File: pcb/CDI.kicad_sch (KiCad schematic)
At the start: 27 parts, among them Q1 MMBT2222A, Q5 MMBT2222A, Q6 MMBT2222A

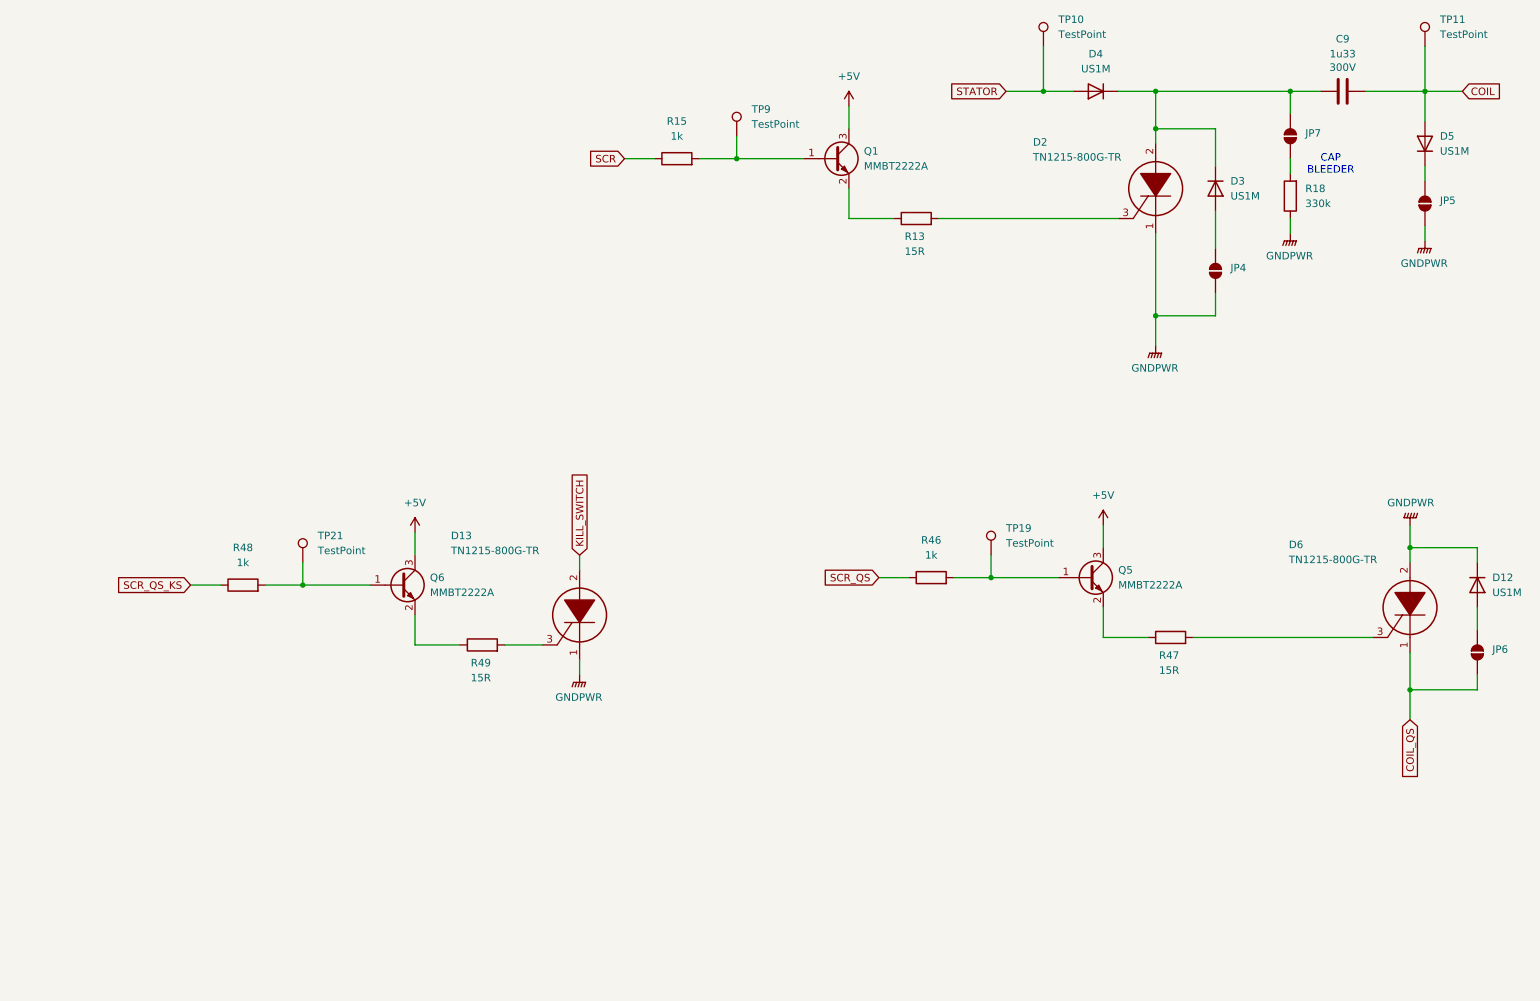
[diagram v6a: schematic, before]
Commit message: changed SCR drives to pnp drive and started schematic revision
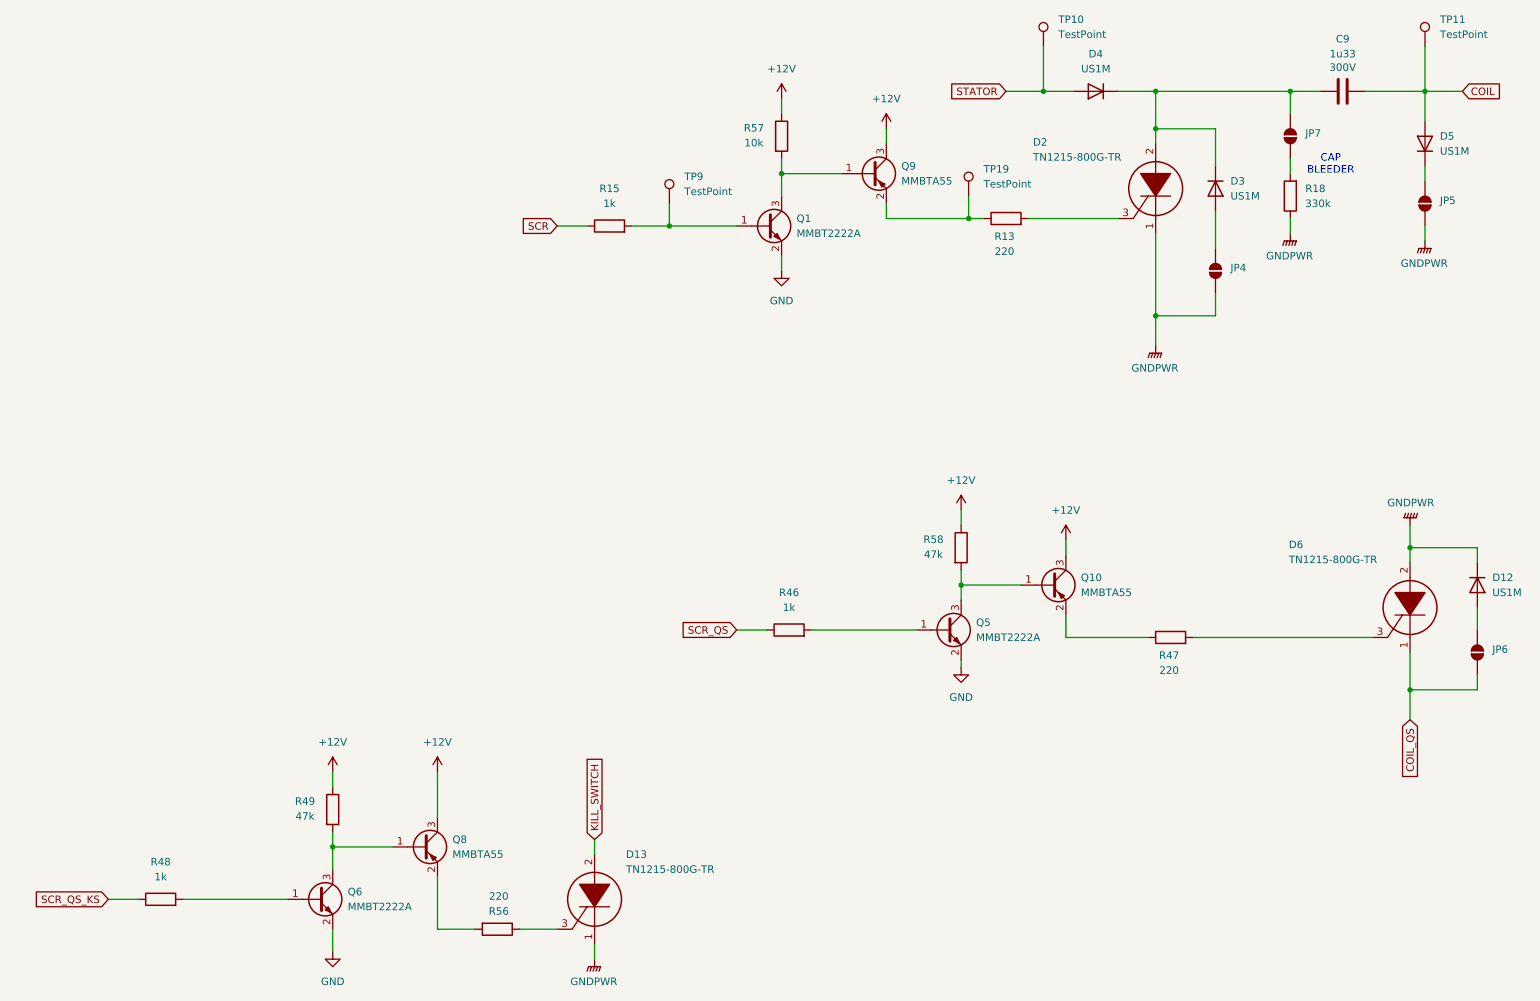
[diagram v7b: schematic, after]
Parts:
- removed TP21: TestPoint, Connector_PinHeader_1.00mm:PinHeader_1x01_P1.00mm_Vertical, symbol Connector:TestPoint
- added Q10, Q8, Q9: MMBTA55, Package_TO_SOT_SMD:SOT-23, symbol Transistor_BJT:MMBTA56
- added R56: 220, Resistor_THT:R_Axial_DIN0204_L3.6mm_D1.6mm_P1.90mm_Vertical, symbol Device:R
- added R57: 10k, Resistor_THT:R_Axial_DIN0204_L3.6mm_D1.6mm_P1.90mm_Vertical, symbol Device:R
- added R58: 47k, Resistor_THT:R_Axial_DIN0204_L3.6mm_D1.6mm_P1.90mm_Vertical, symbol Device:R
- R13, R47: value 15R -> 220
- R49: value 15R -> 47k
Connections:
- net at D13.3: now also R56.1; no longer R49.2
- net +12V: now reaches R49.1
- net +12V: now also Q10.3 (C), Q8.3 (C), Q9.3 (C), R57.1, R58.1; no longer Q6.2 (E)
- net at Q5.1 (B), R46.2: no longer TP19.1
- net at R47.1: now also Q10.2 (E); no longer Q5.2 (E)
- net at R13.1: now also TP19.1, Q9.2 (E); no longer Q1.2 (E)
- removed net +5V: Q1.3 (C), Q5.3 (C), Q6.3 (C)
- new net: Q1.3 (C), Q9.1 (B), R57.2
- new net: Q6.3 (C), Q8.1 (B), R49.2
- new net: Q8.2 (E), R56.2
- new net: Q10.1 (B), Q5.3 (C), R58.2
- new net GND: Q1.2 (E), Q5.2 (E), Q6.2 (E)
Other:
- moved on the sheet: D13, Q1, Q5, Q6, R13, R15, R46, R48, TP19, TP9

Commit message: completed photomos revision
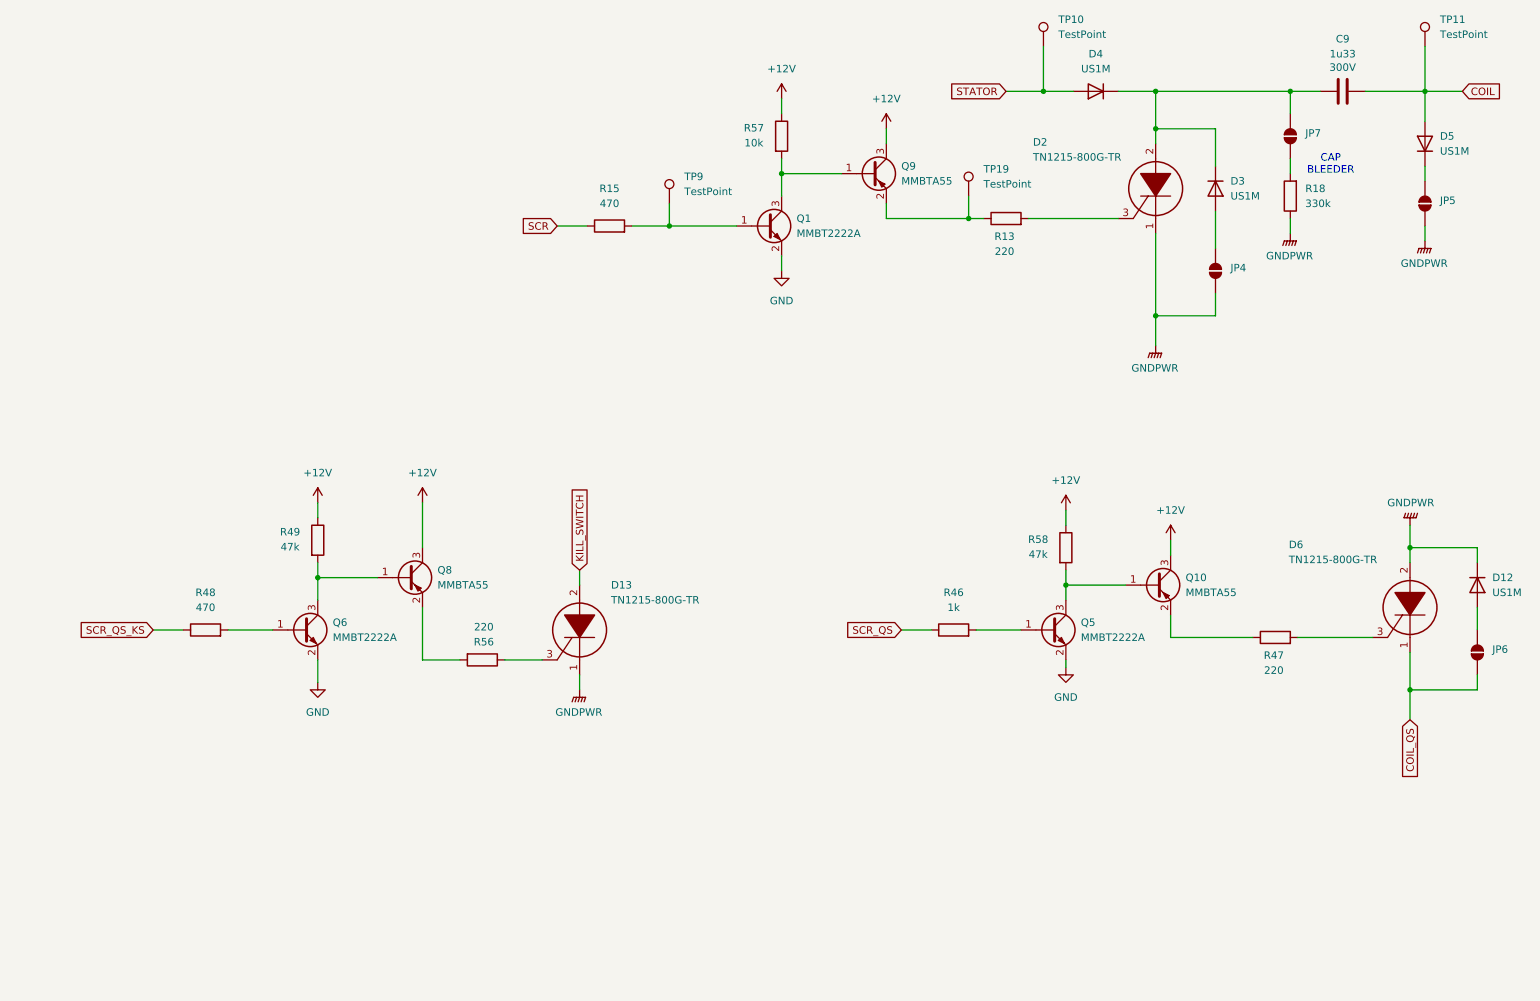
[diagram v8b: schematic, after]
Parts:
- R15, R48: value 1k -> 470
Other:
- moved on the sheet: D13, Q10, Q5, Q6, Q8, R46, R47, R48, R49, R56, R58
